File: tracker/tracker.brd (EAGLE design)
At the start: 100 x 80 mm, 19 parts, among them U1 ATXMEGA128A3-AU, U2 VENUS638FLPX-L

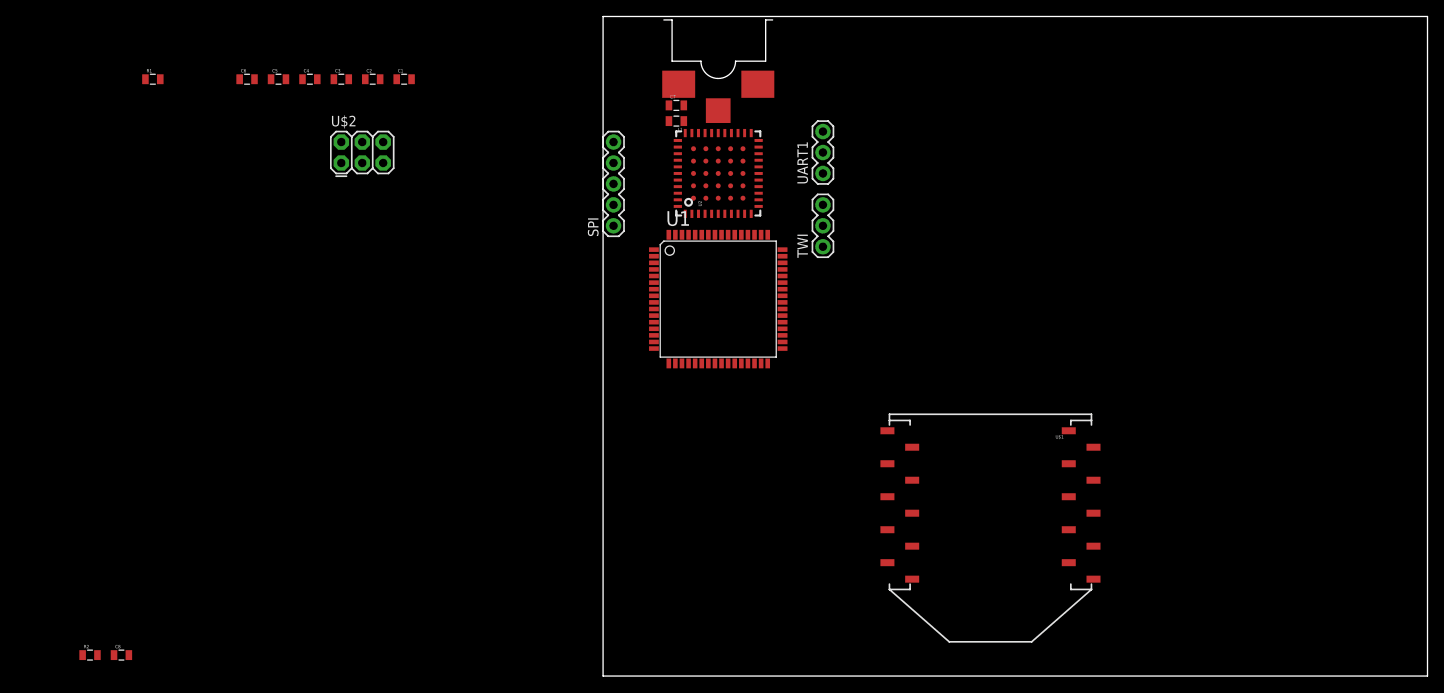
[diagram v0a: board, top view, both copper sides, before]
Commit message: xmega now connected to pdi connector
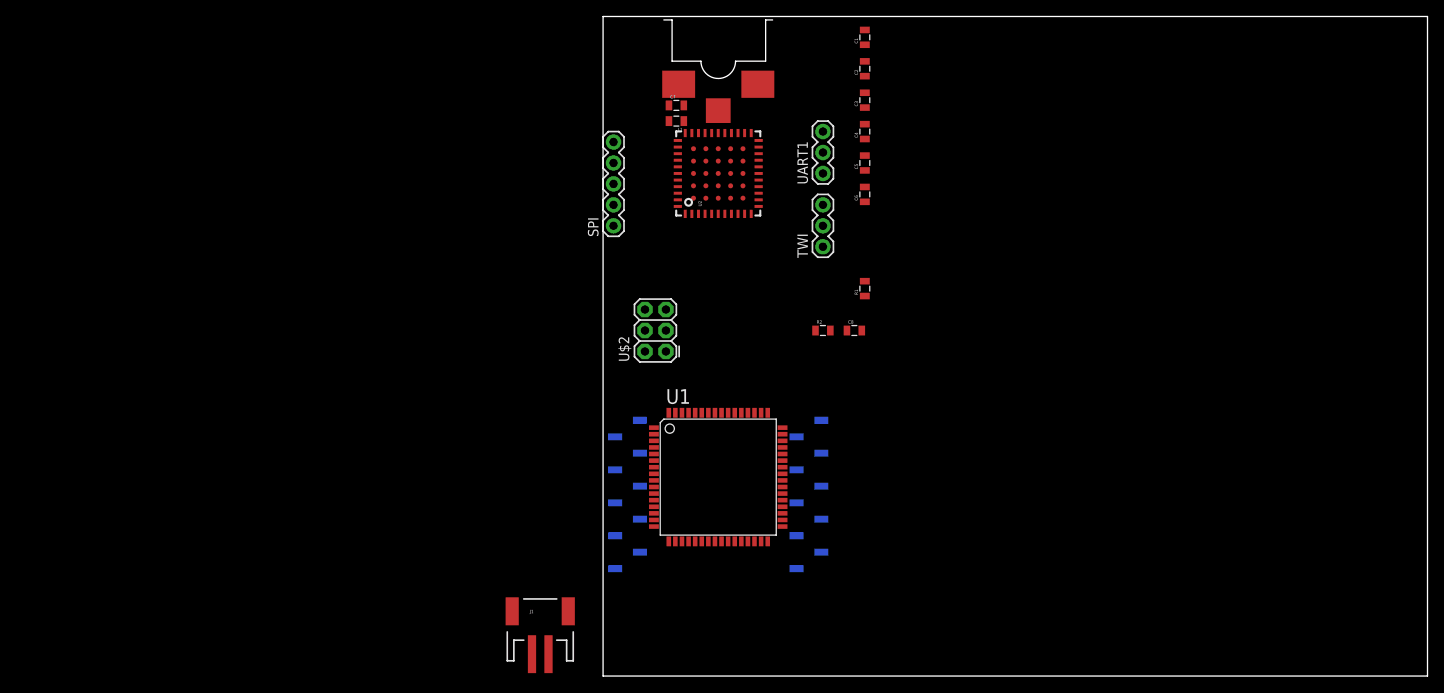
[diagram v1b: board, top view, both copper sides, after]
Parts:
- added J1: (no value), SparkFun-Connectors:JST-2-SMD
- moved C8 97.2 mm to (30.5, 41.9)
- moved R2 97.2 mm to (26.7, 41.9)
- moved R1 90.0 mm to (31.8, 47.0), turned to 90 degrees
- moved C6 76.2 mm to (31.8, 58.4), turned to 90 degrees
- moved C5 71.8 mm to (31.8, 62.2), turned to 90 degrees
- moved C4 67.6 mm to (31.8, 66.0), turned to 90 degrees
- moved C3 63.6 mm to (31.8, 69.8), turned to 90 degrees
- moved C2 59.7 mm to (31.8, 73.7), turned to 90 degrees
- moved C1 56.1 mm to (31.8, 77.5), turned to 90 degrees
- moved U$2 41.6 mm to (6.35, 41.9), turned to 90 degrees
- moved U$1 33.0 mm to (14.0, 33.0), flipped to the bottom
- moved U1 21.6 mm to (14.0, 24.1)
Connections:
- removed net AVCC: U1.61
- removed net VCC: U1.15, U1.25, U1.35, U1.45, U1.53
- new net PDI_CLK: R1.1, U$2.5, U1.57
- new net PDI_DATA: U$2.1, U1.56
- net 3.3V: now also R1.2, U$2.2, U1.15, U1.25, U1.35, U1.45, U1.53, U1.61
- net GND: now also U$2.6

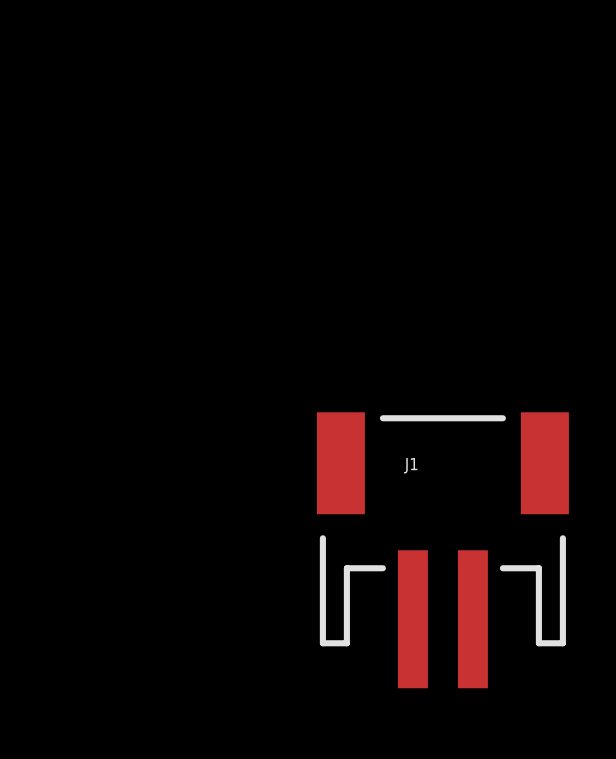
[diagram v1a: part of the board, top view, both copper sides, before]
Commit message: initial steps for the charging/power circuit
 * micro usb port added
 * 2-pin jst battery connector added
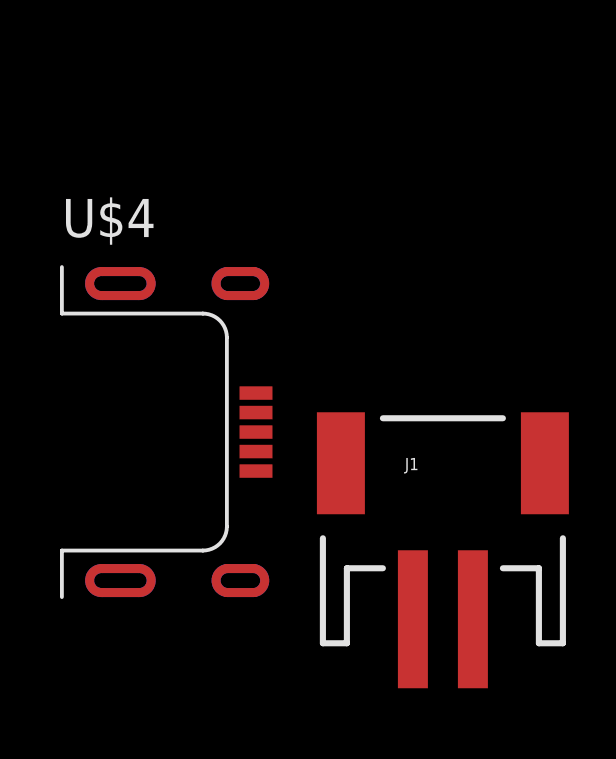
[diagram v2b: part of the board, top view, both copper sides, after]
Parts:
- added U$4: USB, rocket:USB_MICRO_B
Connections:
- new net VIN: U$4.1
- net GND: now also U$4.5
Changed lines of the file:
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@@
 <attribute name="PROD_ID" value="CONN-08352" x="-7.62" y="6.35" size="1.778" layer="27" display="off"/>
 </element>
+<element name="U$4" library="rocket" package="USB_MICRO_B" value="USB" x="-20.32" y="8.89"/>
 </elements>
 <signals>
@@
 <contactref element="UART1" pad="1"/>
 <contactref element="U$2" pad="6"/>
+<contactref element="U$4" pad="5"/>
 <wire x1="31.75" y1="74.56" x2="31.75" y2="78.37" width="0" layer="19" extent="1-1"/>
 <wire x1="31.75" y1="70.75" x2="31.75" y2="74.56" width="0" layer="19" extent="1-1"/>
@@
 <wire x1="13.57" y1="16.33" x2="21.77" y2="18.93" width="0" layer="19" extent="1-1"/>
 <wire x1="6.17" y1="19.73" x2="13.57" y2="16.33" width="0" layer="19" extent="1-1"/>
+<wire x1="-13.85" y1="7.59" x2="6.17" y2="19.73" width="0" layer="19" extent="1-1"/>
 </signal>
 <signal name="VDD">
@@
 <wire x1="7.62" y1="44.45" x2="13.57" y2="31.93" width="0" layer="19" extent="1-1"/>
 </signal>
+<signal name="VIN">
+<contactref element="U$4" pad="1"/>
+</signal>
 </signals>

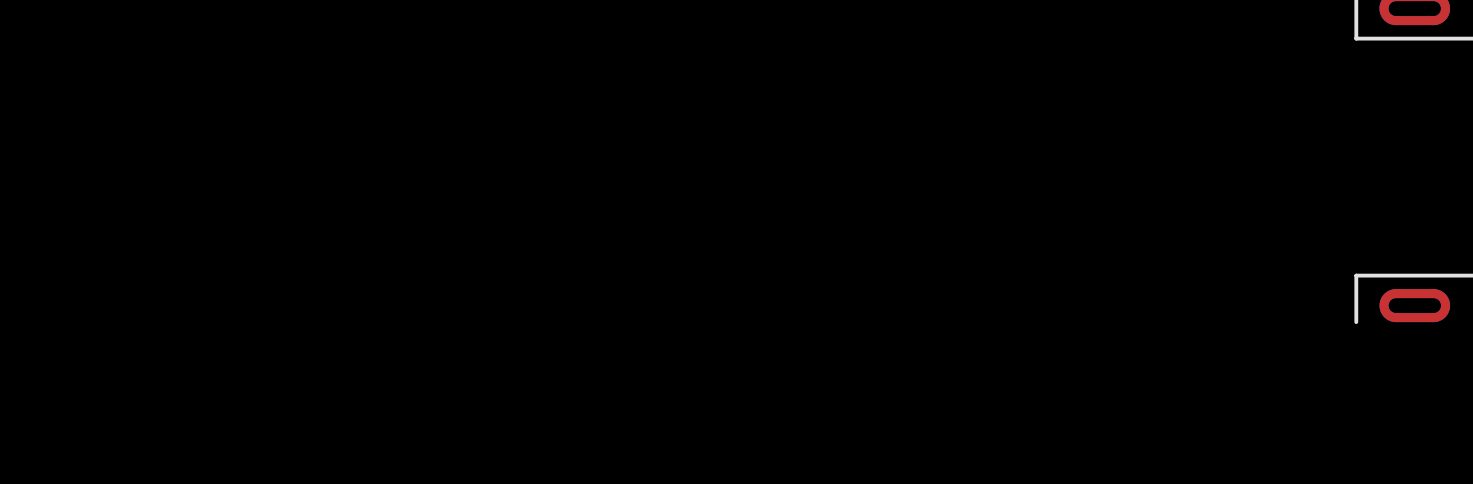
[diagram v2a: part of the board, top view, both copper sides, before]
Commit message: Initial power connection
* Added charging IC
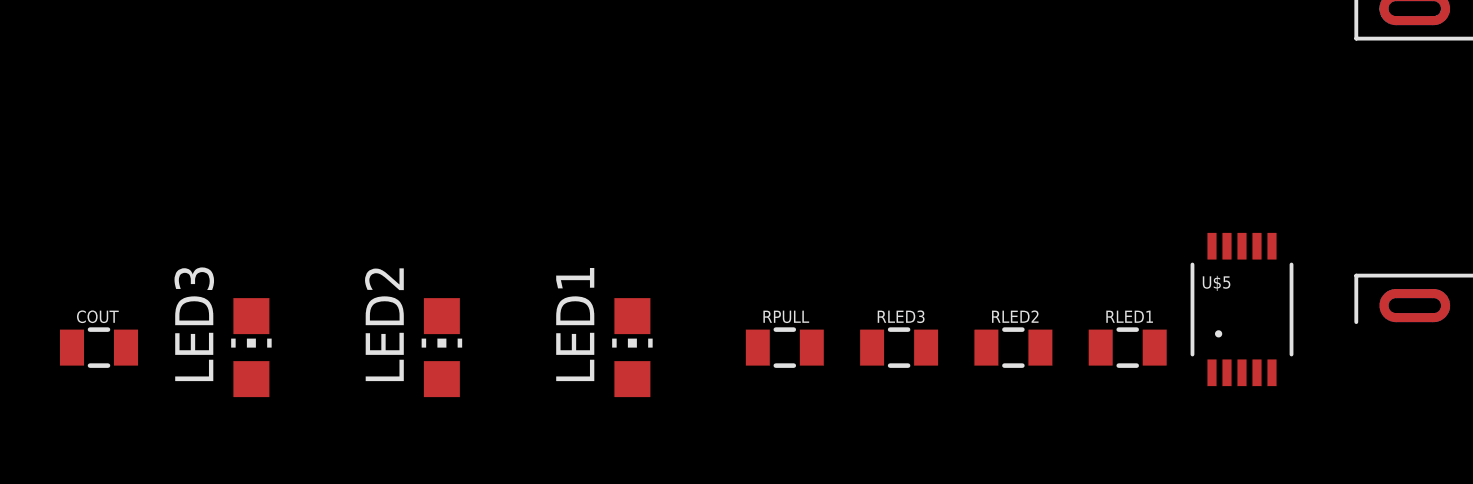
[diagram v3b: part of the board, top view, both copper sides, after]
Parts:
- added COUT: 10 uF, SparkFun:0805
- added LED1, LED2, LED3: (no value), led:CHIP-LED0805
- added RLED1, RLED2, RLED3, RPULL: (no value), SparkFun:0805
- added U$5: MCP73833, rocket:MSOP10
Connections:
- new net N$3: RLED3.1, U$5.7
- new net N$4: RLED2.2, U$5.4
- new net N$5: RLED1.2, U$5.3
- new net N$6: LED1.C, RLED1.1
- new net N$7: LED2.C, RLED2.1
- new net N$8: LED3.C, RLED3.2
- net GND: now also COUT.1, J1.1, RPULL.2, U$5.5
- net VBAT: now also COUT.2, J1.2, U$5.10, U$5.9
- net VIN: now also LED1.A, LED2.A, LED3.A, RPULL.1, U$5.1, U$5.2
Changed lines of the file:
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@@
 </element>
 <element name="U$4" library="rocket" package="USB_MICRO_B" value="USB" x="-20.32" y="8.89"/>
+<element name="U$5" library="rocket" package="MSOP10" value="MCP73833" x="-24.13" y="3.81"/>
+<element name="RLED1" library="SparkFun" package="0805" value="" x="-27.94" y="2.54"/>
+<element name="RLED2" library="SparkFun" package="0805" value="" x="-31.75" y="2.54"/>
+<element name="RLED3" library="SparkFun" package="0805" value="" x="-35.56" y="2.54"/>
+<element name="RPULL" library="SparkFun" package="0805" value="" x="-39.37" y="2.54"/>
+<element name="LED1" library="led" package="CHIP-LED0805" value="" x="-44.45" y="2.54"/>
+<element name="LED2" library="led" package="CHIP-LED0805" value="" x="-50.8" y="2.54"/>
+<element name="LED3" library="led" package="CHIP-LED0805" value="" x="-57.15" y="2.54"/>
+<element name="COUT" library="SparkFun" package="0805" value="10 uF" x="-62.23" y="2.54"/>
 </elements>
 <signals>
@@
 <contactref element="U$2" pad="6"/>
 <contactref element="U$4" pad="5"/>
+<contactref element="U$5" pad="5"/>
+<contactref element="J1" pad="1"/>
+<contactref element="RPULL" pad="2"/>
+<contactref element="COUT" pad="1"/>
 <wire x1="31.75" y1="74.56" x2="31.75" y2="78.37" width="0" layer="19" extent="1-1"/>
 <wire x1="31.75" y1="70.75" x2="31.75" y2="74.56" width="0" layer="19" extent="1-1"/>
@@
 <wire x1="13.57" y1="16.33" x2="21.77" y2="18.93" width="0" layer="19" extent="1-1"/>
 <wire x1="6.17" y1="19.73" x2="13.57" y2="16.33" width="0" layer="19" extent="1-1"/>
-<wire x1="-13.85" y1="7.59" x2="6.17" y2="19.73" width="0" layer="19" extent="1-1"/>
+<wire x1="-8.62" y1="2.65" x2="6.17" y2="19.73" width="0" layer="19" extent="1-1"/>
+<wire x1="-13.85" y1="7.59" x2="-8.62" y2="2.65" width="0" layer="19" extent="1-1"/>
+<wire x1="-23.13" y1="1.7005" x2="-13.85" y2="7.59" width="0" layer="19" extent="1-1"/>
+<wire x1="-38.47" y1="2.54" x2="-23.13" y2="1.7005" width="0" layer="19" extent="1-1"/>
+<wire x1="-63.13" y1="2.54" x2="-38.47" y2="2.54" width="0" layer="19" extent="1-1"/>
 </signal>
 <signal name="VDD">
@@
 <signal name="VBAT">
 <contactref element="U2" pad="18"/>
+<contactref element="COUT" pad="2"/>
+<contactref element="U$5" pad="10"/>
+<contactref element="U$5" pad="9"/>
+<contactref element="J1" pad="2"/>
+<wire x1="-6.62" y1="2.65" x2="18.87" y2="61.76" width="0" layer="19" extent="1-1"/>
+<wire x1="-24.63" y1="5.9195" x2="-6.62" y2="2.65" width="0" layer="19" extent="1-1"/>
+<wire x1="-25.13" y1="5.9195" x2="-24.63" y2="5.9195" width="0" layer="19" extent="1-1"/>
+<wire x1="-61.33" y1="2.54" x2="-25.13" y2="5.9195" width="0" layer="19" extent="1-1"/>
 </signal>
 <signal name="RSTN">
@@
 <signal name="VIN">
 <contactref element="U$4" pad="1"/>
+<contactref element="U$5" pad="1"/>
+<contactref element="U$5" pad="2"/>
+<contactref element="LED2" pad="A"/>
+<contactref element="LED1" pad="A"/>
+<contactref element="LED3" pad="A"/>
+<contactref element="RPULL" pad="1"/>
+<wire x1="-50.8" y1="1.49" x2="-57.15" y2="1.49" width="0" layer="19" extent="1-1"/>
+<wire x1="-44.45" y1="1.49" x2="-50.8" y2="1.49" width="0" layer="19" extent="1-1"/>
+<wire x1="-40.27" y1="2.54" x2="-44.45" y2="1.49" width="0" layer="19" extent="1-1"/>
+<wire x1="-25.13" y1="1.7005" x2="-40.27" y2="2.54" width="0" layer="19" extent="1-1"/>
+<wire x1="-24.63" y1="1.7005" x2="-25.13" y2="1.7005" width="0" layer="19" extent="1-1"/>
+<wire x1="-13.85" y1="10.19" x2="-24.63" y2="1.7005" width="0" layer="19" extent="1-1"/>
+</signal>
+<signal name="N$4">
+<contactref element="RLED2" pad="2"/>
+<contactref element="U$5" pad="4"/>
+<wire x1="-23.63" y1="1.7005" x2="-30.85" y2="2.54" width="0" layer="19" extent="1-1"/>
+</signal>
+<signal name="N$5">
+<contactref element="U$5" pad="3"/>
+<contactref element="RLED1" pad="2"/>
+<wire x1="-27.04" y1="2.54" x2="-24.13" y2="1.7005" width="0" layer="19" extent="1-1"/>
+</signal>
+<signal name="N$3">
+<contactref element="U$5" pad="7"/>
+<contactref element="RLED3" pad="1"/>
+<wire x1="-23.63" y1="5.9195" x2="-36.46" y2="2.54" width="0" layer="19" extent="1-1"/>
+</signal>
+<signal name="N$6">
+<contactref element="LED1" pad="C"/>
+<contactref element="RLED1" pad="1"/>
+<wire x1="-28.84" y1="2.54" x2="-44.45" y2="3.59" width="0" layer="19" extent="1-1"/>
+</signal>
+<signal name="N$7">
+<contactref element="LED2" pad="C"/>
+<contactref element="RLED2" pad="1"/>
+<wire x1="-32.65" y1="2.54" x2="-50.8" y2="3.59" width="0" layer="19" extent="1-1"/>
+</signal>
+<signal name="N$8">
+<contactref element="RLED3" pad="2"/>
+<contactref element="LED3" pad="C"/>
+<wire x1="-34.66" y1="2.54" x2="-57.15" y2="3.59" width="0" layer="19" extent="1-1"/>
 </signal>
 </signals>

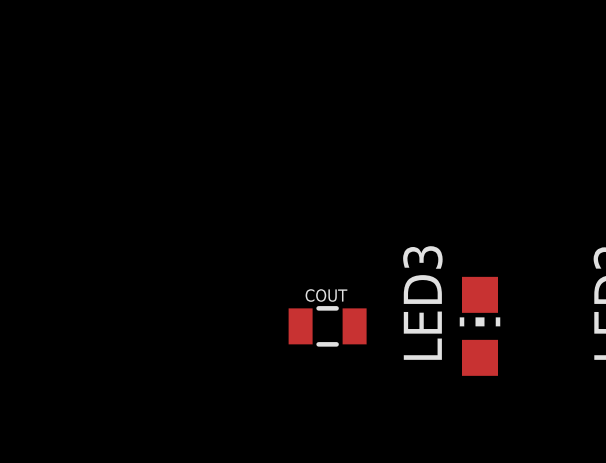
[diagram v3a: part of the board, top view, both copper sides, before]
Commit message: Updates to charging circuit
* completed all connections for the charging circuit, except the
thermistor as it is still undecided how we will deal with that.
* still need to choose a voltage regulator and add it between the
battery and main circuit.
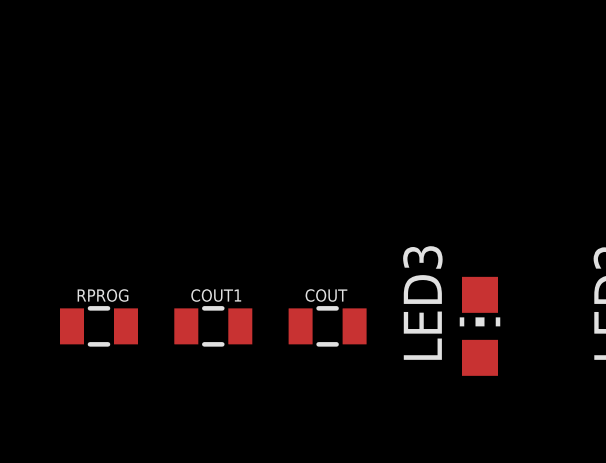
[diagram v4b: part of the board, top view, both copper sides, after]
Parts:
- added COUT1: 10 uF, SparkFun:0805
- added RPROG: 1K, SparkFun:0805
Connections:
- new net N$12: RPROG.2, U$5.6
- net GND: now also COUT1.1, RPROG.1
- net VIN: now also COUT1.2
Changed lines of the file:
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@@
 <element name="LED3" library="led" package="CHIP-LED0805" value="" x="-57.15" y="2.54"/>
 <element name="COUT" library="SparkFun" package="0805" value="10 uF" x="-62.23" y="2.54"/>
+<element name="COUT1" library="SparkFun" package="0805" value="10 uF" x="-66.04" y="2.54"/>
+<element name="RPROG" library="SparkFun" package="0805" value="1K" x="-69.85" y="2.54"/>
 </elements>
 <signals>
@@
 <contactref element="RPULL" pad="2"/>
 <contactref element="COUT" pad="1"/>
+<contactref element="COUT1" pad="1"/>
+<contactref element="RPROG" pad="1"/>
 <wire x1="31.75" y1="74.56" x2="31.75" y2="78.37" width="0" layer="19" extent="1-1"/>
 <wire x1="31.75" y1="70.75" x2="31.75" y2="74.56" width="0" layer="19" extent="1-1"/>
@@
 <wire x1="-38.47" y1="2.54" x2="-23.13" y2="1.7005" width="0" layer="19" extent="1-1"/>
 <wire x1="-63.13" y1="2.54" x2="-38.47" y2="2.54" width="0" layer="19" extent="1-1"/>
+<wire x1="-66.94" y1="2.54" x2="-63.13" y2="2.54" width="0" layer="19" extent="1-1"/>
+<wire x1="-70.75" y1="2.54" x2="-66.94" y2="2.54" width="0" layer="19" extent="1-1"/>
 </signal>
 <signal name="VDD">
@@
 <contactref element="LED3" pad="A"/>
 <contactref element="RPULL" pad="1"/>
+<contactref element="COUT1" pad="2"/>
+<wire x1="-57.15" y1="1.49" x2="-65.14" y2="2.54" width="0" layer="19" extent="1-1"/>
 <wire x1="-50.8" y1="1.49" x2="-57.15" y2="1.49" width="0" layer="19" extent="1-1"/>
 <wire x1="-44.45" y1="1.49" x2="-50.8" y2="1.49" width="0" layer="19" extent="1-1"/>
@@
 <wire x1="-34.66" y1="2.54" x2="-57.15" y2="3.59" width="0" layer="19" extent="1-1"/>
 </signal>
+<signal name="N$12">
+<contactref element="U$5" pad="6"/>
+<contactref element="RPROG" pad="2"/>
+<wire x1="-23.13" y1="5.9195" x2="-68.95" y2="2.54" width="0" layer="19" extent="1-1"/>
+</signal>
 </signals>
